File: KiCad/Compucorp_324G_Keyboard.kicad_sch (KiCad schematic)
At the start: 49 parts, among them J3 To Scan Board, SW1 e^x 10^x, SW10 2nd FUNC, SW11 ARCTAN, SW12 a^x, SW13 5, SW14 EXCHn, SW15 START/STOP, SW16 x,y → Θ,r, SW17 DIV, SW18 EXP, SW19 4, SW2 ), SW20 RCLn, SW21 CLEAR ENTRY, SW22 º → R → º, SW23 ARCSIN ARCCOS, SW24 MUL, SW25 CHG SIGN, SW26 3, SW27 STn, SW28 RESET, SW29 TAN, SW3 DEC → D.MS, SW30 INV, SW31 MINUS, SW32 DP, SW33 2, SW34 Θ,r → x,y, SW35 SQRT, SW36 PLUS, SW37 9, SW38 1, SW39 SIN COS, SW4 7, SW40 PI, SW41 EQUALS, SW42 8, SW43 0, SW44 FED/MUNI, SW45 RUN/LOAD, SW46 PROG 1/2, SW47 RUN/STEP/LOAD, SW48 GRAD/DEG, SW5 Ln LOG, SW6 (, SW7 D.MS → DEC, SW8 6, SW9 SET DP

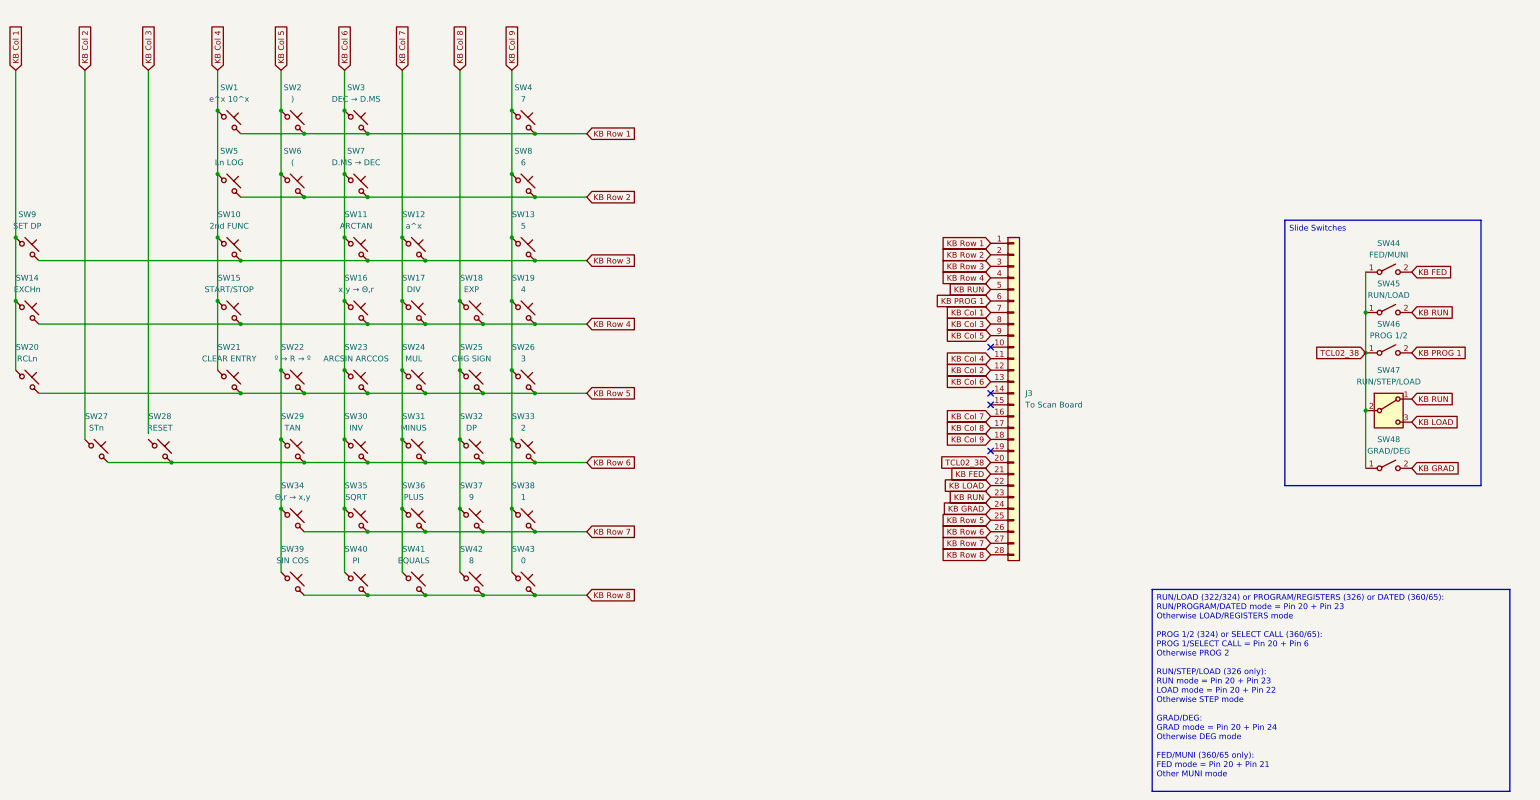
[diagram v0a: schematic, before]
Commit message: Update Compucorp_324G_Keyboard.kicad_sch
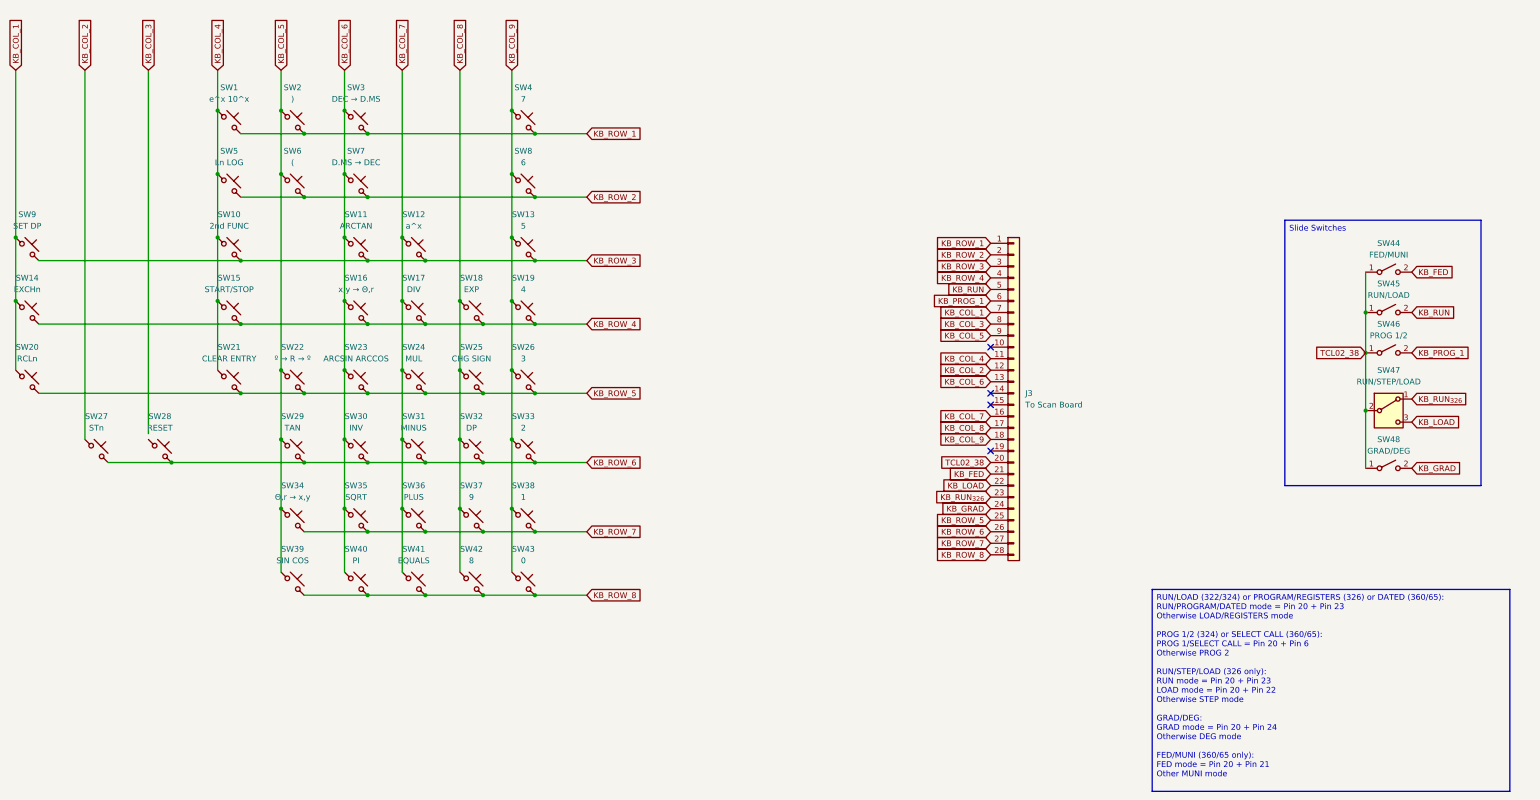
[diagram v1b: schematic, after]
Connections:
- net KB Col 1 renamed KB_COL_1
- net KB Col 2 renamed KB_COL_2
- net KB Col 3 renamed KB_COL_3
- net KB Col 4 renamed KB_COL_4
- net KB Col 5 renamed KB_COL_5
- net KB Col 6 renamed KB_COL_6
- net KB Col 7 renamed KB_COL_7
- net KB Col 8 renamed KB_COL_8
- net KB Col 9 renamed KB_COL_9
- net KB FED renamed KB_FED
- net KB GRAD renamed KB_GRAD
- net KB LOAD renamed KB_LOAD
- net KB PROG 1 renamed KB_PROG_1
- net KB RUN renamed KB_RUN
- net KB_RUN: no longer J3.23 (Pin_23), SW47.1 (A)
- net KB Row 1 renamed KB_ROW_1
- net KB Row 2 renamed KB_ROW_2
- net KB Row 3 renamed KB_ROW_3
- net KB Row 4 renamed KB_ROW_4
- net KB Row 5 renamed KB_ROW_5
- net KB Row 6 renamed KB_ROW_6
- net KB Row 7 renamed KB_ROW_7
- net KB Row 8 renamed KB_ROW_8
- new net KB_RUN_{326}: J3.23 (Pin_23), SW47.1 (A)
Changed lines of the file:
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@@
 		)
 	)
-	(global_label "KB Row 3"
+	(global_label "KB_ROW_3"
 		(shape input)
 		(at 193.04 127 0)
@@
 		)
 	)
-	(global_label "KB Row 5"
+	(global_label "KB_ROW_5"
 		(shape input)
 		(at 193.04 156.21 0)
@@
 		)
 	)
-	(global_label "KB Col 6"
+	(global_label "KB_COL_6"
 		(shape input)
 		(at 139.7 85.09 90)
@@
 		)
 	)
-	(global_label "KB Row 7"
+	(global_label "KB_ROW_7"
 		(shape input)
 		(at 193.04 186.69 0)
@@
 		)
 	)
-	(global_label "KB Col 5"
+	(global_label "KB_COL_5"
 		(shape input)
 		(at 125.73 85.09 90)
@@
 		)
 	)
-	(global_label "KB Col 3"
+	(global_label "KB_COL_3"
 		(shape input)
 		(at 96.52 85.09 90)
@@
 		)
 	)
-	(global_label "KB Row 8"
+	(global_label "KB_ROW_8"
 		(shape input)
 		(at 193.04 200.66 0)
@@
 		)
 	)
-	(global_label "KB Row 2"
+	(global_label "KB_ROW_2"
 		(shape input)
 		(at 193.04 113.03 0)
@@
 		)
 	)
-	(global_label "KB RUN"
+	(global_label "KB_RUN_{326}"
 		(shape input)
 		(at 374.65 157.48 0)
@@
 		)
 		(property "Intersheetrefs" "${INTERSHEET_REFS}"
-			(at 385.0738 157.48 0)
-			(effects
-				(font
-					(size 1.27 1.27)
-				)
-				(justify left)
-				(hide yes)
-			)
-		)
-	)
-	(global_label "KB GRAD"
+			(at 388.0274 157.48 0)
+			(effects
+				(font
+					(size 1.27 1.27)
+				)
+				(justify left)
+				(hide yes)
+			)
+		)
+	)
+	(global_label "KB_GRAD"
 		(shape input)
 		(at 374.65 172.72 0)
@@
 		)
 	)
-	(global_label "KB RUN"
+	(global_label "KB_RUN"
 		(shape input)
 		(at 374.65 138.43 0)
@@
 		)
 	)
-	(global_label "KB FED"
+	(global_label "KB_FED"
 		(shape input)
 		(at 374.65 129.54 0)
@@
 		)
 	)
-	(global_label "KB Col 2"
+	(global_label "KB_COL_2"
 		(shape input)
 		(at 82.55 85.09 90)
@@
 		)
 	)
-	(global_label "KB LOAD"
+	(global_label "KB_LOAD"
 		(shape input)
 		(at 374.65 162.56 0)
@@
 		)
 	)
-	(global_label "KB Col 7"
+	(global_label "KB_COL_7"
 		(shape input)
 		(at 152.4 85.09 90)
@@
 		)
 	)
-	(global_label "KB Row 6"
+	(global_label "KB_ROW_6"
 		(shape input)
 		(at 193.04 171.45 0)
@@
 		)
 	)
-	(global_label "KB Col 9"
+	(global_label "KB_COL_9"
 		(shape input)
 		(at 176.53 85.09 90)
@@
 		)
 	)
-	(global_label "KB Row 4"
+	(global_label "KB_ROW_4"
 		(shape input)
 		(at 193.04 140.97 0)
@@
 		)
 	)
-	(global_label "KB PROG 1"
+	(global_label "KB_PROG_1"
 		(shape input)
 		(at 374.65 147.32 0)
@@
 		)
 	)
-	(global_label "KB Col 8"
+	(global_label "KB_COL_8"
 		(shape input)
 		(at 165.1 85.09 90)
@@
 		)
 	)
-	(global_label "KB Col 1"
+	(global_label "KB_COL_1"
 		(shape input)
 		(at 67.31 85.09 90)
@@
 		)
 	)
-	(global_label "KB Row 1"
+	(global_label "KB_ROW_1"
 		(shape input)
 		(at 193.04 99.06 0)
@@
 		)
 	)
-	(global_label "KB Row 3"
+	(global_label "KB_ROW_3"
 		(shape input)
 		(at 281.94 128.27 180)
@@
 		)
 	)
-	(global_label "KB Row 4"
+	(global_label "KB_ROW_4"
 		(shape input)
 		(at 281.94 130.81 180)
@@
 		)
 	)
-	(global_label "KB Row 1"
+	(global_label "KB_ROW_1"
 		(shape input)
 		(at 281.94 123.19 180)
@@
 		)
 	)
-	(global_label "KB Row 2"
+	(global_label "KB_ROW_2"
 		(shape input)
 		(at 281.94 125.73 180)
@@
 		)
 	)
-	(global_label "KB RUN"
+	(global_label "KB_RUN"
 		(shape input)
 		(at 281.94 133.35 180)
@@
 		)
 	)
-	(global_label "KB PROG 1"
+	(global_label "KB_PROG_1"
 		(shape input)
 		(at 281.94 135.89 180)
@@
 		)
 	)
-	(global_label "KB Col 3"
+	(global_label "KB_COL_3"
 		(shape input)
 		(at 281.94 140.97 180)
@@
 		)
 	)
-	(global_label "KB Col 1"
+	(global_label "KB_COL_1"
 		(shape input)
 		(at 281.94 138.43 180)
@@
 		)
 	)
-	(global_label "KB Col 5"
+	(global_label "KB_COL_5"
 		(shape input)
 		(at 281.94 143.51 180)
@@
 		)
 	)
-	(global_label "KB Col 7"
+	(global_label "KB_COL_7"
 		(shape input)
 		(at 281.94 161.29 180)
@@
 		)
 	)
-	(global_label "KB Col 8"
+	(global_label "KB_COL_8"
 		(shape input)
 		(at 281.94 163.83 180)
@@
 		)
 	)
-	(global_label "KB Col 4"
+	(global_label "KB_COL_4"
 		(shape input)
 		(at 281.94 148.59 180)
@@
 		)
 	)
-	(global_label "KB Col 2"
+	(global_label "KB_COL_2"
 		(shape input)
 		(at 281.94 151.13 180)
@@
 		)
 	)
-	(global_label "KB Col 6"
+	(global_label "KB_COL_6"
 		(shape input)
 		(at 281.94 153.67 180)
@@
 		)
 	)
-	(global_label "KB Col 9"
+	(global_label "KB_COL_9"
 		(shape input)
 		(at 281.94 166.37 180)
@@
 		)
 	)
-	(global_label "KB GRAD"
+	(global_label "KB_GRAD"
 		(shape input)
 		(at 281.94 181.61 180)
@@
 		)
 	)
-	(global_label "KB Row 5"
+	(global_label "KB_ROW_5"
 		(shape input)
 		(at 281.94 184.15 180)
@@
 		)
 	)
-	(global_label "KB Row 6"
+	(global_label "KB_ROW_6"
 		(shape input)
 		(at 281.94 186.69 180)
@@
 		)
 	)
-	(global_label "KB Row 7"
+	(global_label "KB_ROW_7"
 		(shape input)
 		(at 281.94 189.23 180)
@@
 		)
 	)
-	(global_label "KB Row 8"
+	(global_label "KB_ROW_8"
 		(shape input)
 		(at 281.94 191.77 180)
@@
 		)
 	)
-	(global_label "KB RUN"
+	(global_label "KB_RUN_{326}"
 		(shape input)
 		(at 281.94 179.07 180)
@@
 		)
 		(property "Intersheetrefs" "${INTERSHEET_REFS}"
-			(at 271.5162 179.07 0)
-			(effects
-				(font
-					(size 1.27 1.27)
-				)
-				(justify right)
-				(hide yes)
-			)
-		)
-	)
-	(global_label "KB LOAD"
+			(at 268.5626 179.07 0)
+			(effects
+				(font
+					(size 1.27 1.27)
+				)
+				(justify right)
+				(hide yes)
+			)
+		)
+	)
+	(global_label "KB_LOAD"
 		(shape input)
 		(at 281.94 176.53 180)
@@
 		)
 	)
-	(global_label "KB FED"
+	(global_label "KB_FED"
 		(shape input)
 		(at 281.94 173.99 180)
@@
 		)
 	)
-	(global_label "KB Col 4"
+	(global_label "KB_COL_4"
 		(shape input)
 		(at 111.76 85.09 90)

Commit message: Update Compucorp_324G_Keyboard.kicad_sch
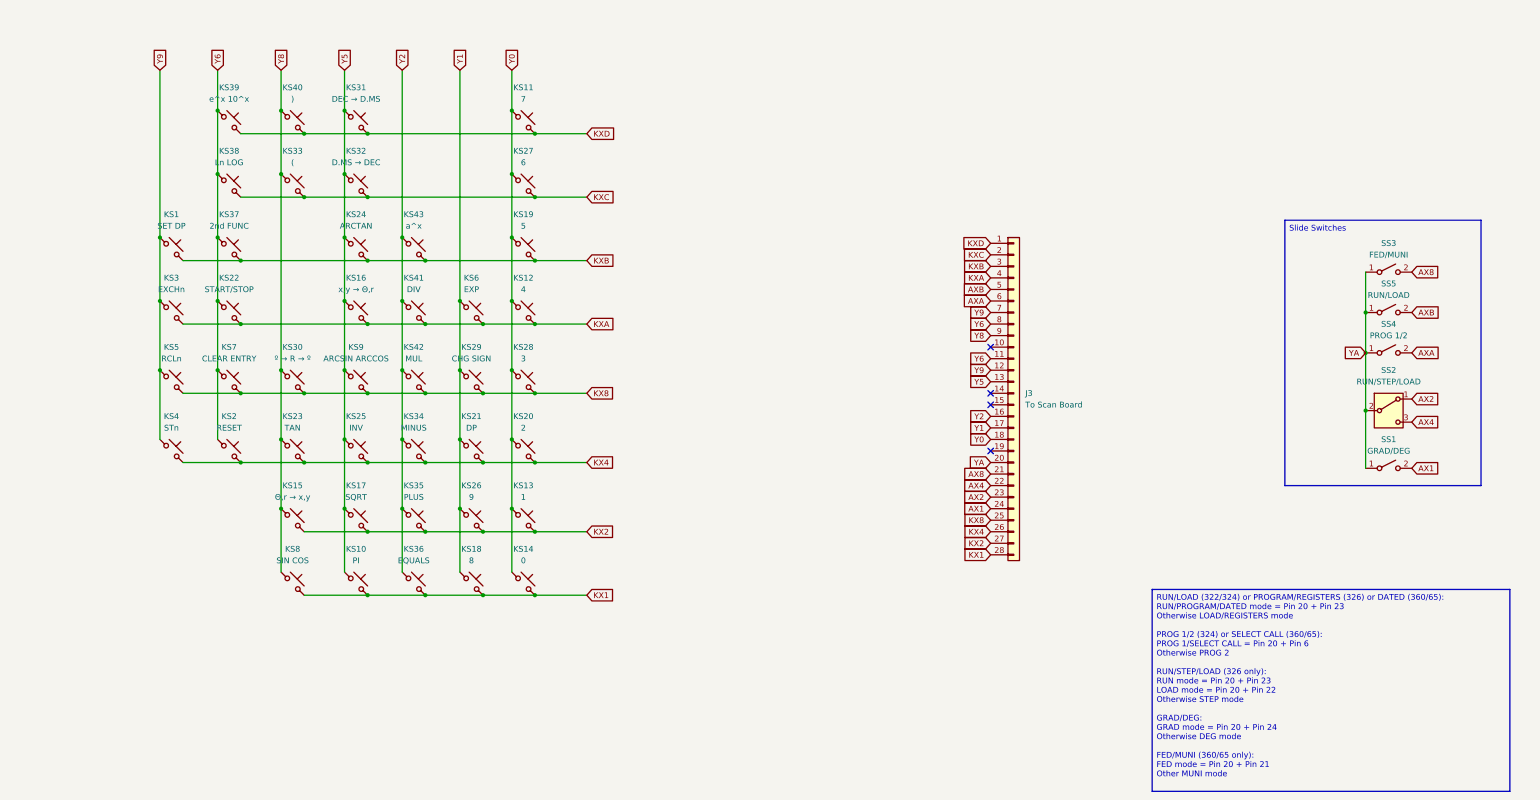
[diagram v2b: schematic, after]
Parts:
- renumbered SW9 to KS1, SW40 to KS10, SW4 to KS11, SW19 to KS12, SW38 to KS13, SW43 to KS14, SW34 to KS15, SW16 to KS16, SW35 to KS17, SW42 to KS18, SW13 to KS19, SW28 to KS2, SW33 to KS20, SW32 to KS21, SW15 to KS22, SW29 to KS23, SW11 to KS24, SW30 to KS25, SW37 to KS26, SW8 to KS27, SW26 to KS28, SW25 to KS29, SW14 to KS3, SW22 to KS30, SW3 to KS31, SW7 to KS32, SW6 to KS33, SW31 to KS34, SW36 to KS35, SW41 to KS36, SW10 to KS37, SW5 to KS38, SW1 to KS39, SW27 to KS4, SW2 to KS40, SW17 to KS41, SW24 to KS42, SW12 to KS43, SW20 to KS5, SW18 to KS6, SW21 to KS7, SW39 to KS8, SW23 to KS9, SW48 to SS1, SW47 to SS2, SW44 to SS3, SW46 to SS4, SW45 to SS5
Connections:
- net KB_COL_2 is gone; now on net Y9: J3.12 (Pin_12), KS4.1
- net KB_COL_3 is gone; now on net Y6: J3.8 (Pin_8)
- net KB_COL_4 is gone; now on net Y6: J3.11 (Pin_11), KS22.1, KS37.1, KS38.1, KS39.1, KS7.1
- net Y6: now reaches KS2.1
- net KB_COL_1 renamed Y9
- net KB_COL_5 renamed Y8
- net KB_COL_6 renamed Y5
- net KB_COL_7 renamed Y2
- net KB_COL_8 renamed Y1
- net KB_COL_9 renamed Y0
- net KB_FED renamed AX8
- net KB_GRAD renamed AX1
- net KB_LOAD renamed AX4
- net KB_PROG_1 renamed AXA
- net KB_ROW_1 renamed KXD
- net KB_ROW_2 renamed KXC
- net KB_ROW_3 renamed KXB
- net KB_ROW_4 renamed KXA
- net KB_ROW_5 renamed KX8
- net KB_ROW_6 renamed KX4
- net KB_ROW_7 renamed KX2
- net KB_ROW_8 renamed KX1
- net KB_RUN renamed AXB
- net KB_RUN_{326} renamed AX2
- net TCL02_38 renamed YA
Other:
- moved on the sheet: KS1, KS2, KS3, KS4, KS5
